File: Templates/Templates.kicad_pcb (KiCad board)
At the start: 0 parts

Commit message: update:添加文件
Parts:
- added BAT1: CR2032, DuRuofu_Connector:BAT-TH_BS-2-1, F.Cu at (105.1, 46.4)
- added J1: DC-005, EXT_Connectors_THT:DC-005, F.Cu at (107.6, 59.8)
- added J10: ~, EXT_Other:ANT-SMD_L3.1-W1.6, F.Cu at (135.4, 108.8)
- added J2: ~, Connector_Coaxial:U.FL_Hirose_U.FL-R-SMT-1_Vertical, F.Cu at (148.0, 43.9)
- added J3: Micro_SD_Card, EXT_Connectors_SMD:自弹式micro-SD卡(TF卡)卡座-外焊式, F.Cu at (124.4, 80.6)
- added J4: ~, EXT_Connectors_SMD:自弹式micro-SIM卡-卡座-6P-SIM卡连接器SMD, F.Cu at (126.3, 49.7)
- added J5: ~, EXT_Connectors_THT:SMA-KWE, F.Cu at (140.6, 53.4)
- added J6: ~, EXT_Connectors_THT:CONN-TH_2P-P5.08, F.Cu at (107.8, 79.6)
- added J7: ~, EXT_Connectors_THT:CONN-TH_3P-P5.08, F.Cu at (142.7, 79.6)
- added J8: ~, EXT_Connectors_THT:CONN-TH_4P-P5.08_KF2EDGRC-5.08-4P, F.Cu at (128.4, 61.3)
- added J9: OK-14F024-04, EXT_Connectors_SMD:亚奇连接器-OK-14F024-04, F.Cu at (98.2, 79.6)
- added K1: G6K-2F-Y_DC5, DuRuofu_Switch:G6K-2F-Y DC5, F.Cu at (125.2, 97.5)
- added K2: HF32F-G-HS, EXT_Switch_THT:HF32F-G-HS, F.Cu at (103.1, 124.0)
- added OLED1: OLED_0.96, EXT_Modules:0.96OLED_4P, F.Cu at (168.6, 34.4)
- added Q1: S8050, Package_TO_SOT_SMD:SOT-23, F.Cu at (134.8, 116.0)
- added U1: ~, EXT_Connectors_THT:CONN-TH_XY2500V-F-3.5-8P, F.Cu at (131.9, 37.2)
- added U10: ~, Package_LGA:Bosch_LGA-14_3x2.5mm_P0.5mm, F.Cu at (190.5, 111.9)
- added U11: ~, EXT_IC_SMD:SMD-4_4.6x7.62mm_P2.54mm, F.Cu at (183.6, 106.5)
- added U12: RG-02, EXT_IC_SMD:GPS-SMD_GP-02, F.Cu at (189.2, 92.6)
- added U13: L9119S, Package_SO:SOP-8_5.28x5.23mm_P1.27mm, F.Cu at (182.8, 113.0)
- added U14: ~, EXT_IC_SMD:Maxim_OLGA-14_3.3x5.6mm_P0.8mm, F.Cu at (175.0, 125.6)
- added U15: MAX98357A, EXT_IC_SMD:TQFN-16-1EP_3x3mm_P0.5mm_EP1.23x1.23mm, F.Cu at (180.2, 125.7)
- added U16: Ra-01SC, EXT_IC_SMD:COMM-SMD_RA-01S, F.Cu at (162.5, 116.6)
- added U17: SGM2209, Package_TO_SOT_SMD:SOT-23-5, F.Cu at (175.0, 105.8)
- added U18: SGM2211, Package_TO_SOT_SMD:SOT-23-5, F.Cu at (175.0, 110.5)
- added U19: SGM2212-3.3XKC3G/TR, Package_TO_SOT_SMD:SOT-223, F.Cu at (177.4, 91.0)
- added U2: ~, EXT_Modules:MPU6050-GY-521, F.Cu at (185.0, 33.0)
- added U20: SGM2212-5.0XKC3G/TR, Package_TO_SOT_SMD:SOT-223, F.Cu at (177.4, 99.3)
- added U21: SGM3209YS8G/TR, Package_SO:HSOP-8-1EP_3.9x4.9mm_P1.27mm_EP2.41x3.1mm, F.Cu at (190.4, 126.4)
- added U22: SGM6601, Package_TO_SOT_SMD:TSOT-23-5, F.Cu at (175.0, 115.1)
- added U23: ~, Package_TO_SOT_SMD:SOT-23-6, F.Cu at (175.0, 119.7)
- added U24: TP4056, EXT_IC_SMD:EPSOP-8, F.Cu at (190.4, 119.8)
- added U25: TPS5430DDA, Package_SO:TI_SO-PowerPAD-8_ThermalVias, F.Cu at (181.9, 119.8)
- added U26: ~, EXT_Switch_THT:SW_Push_1P1T_NO_6x6mm, F.Cu at (118.5, 122.1)
- added U27: ~, EXT_Switch_THT:热插拔键盘轴(RGB反贴)(30mm), F.Cu at (106.7, 105.0)
- added U3: ~, EXT_Modules:MQ-2, F.Cu at (159.9, 69.4)
- added U4: ~, EXT_Modules:SW-TH_THB001P, F.Cu at (183.0, 73.6)
- added U5: ~, EXT_Other:Buzzer, F.Cu at (136.2, 99.4)
- added U6: AIR780EX, EXT_IC_SMD:LCC-54_L17.7-W15.8-P1.10_AIR780EX, F.Cu at (163.1, 97.1)
- added U7: ~, EXT_IC_SMD:WSOF-6_L2.6-W1.6-P0.50-TL-EP, F.Cu at (184.9, 99.9)
- added U8: ~, Package_LGA:Bosch_LGA-8_2.5x2.5mm_P0.65mm_ClockwisePinNumbering, F.Cu at (191.8, 105.7)
- added U9: ~, EXT_IC_SMD:WLCSP-12_1.56x1.56mm_P0.4mm, F.Cu at (189.1, 100.4)
- added X1: YSX321SL, Crystal:Crystal_SMD_SeikoEpson_FA238-4Pin_3.2x2.5mm, F.Cu at (141.0, 109.3)
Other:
- board outline added: 115.6 x 106.7 mm
- copper layers 0 -> 2

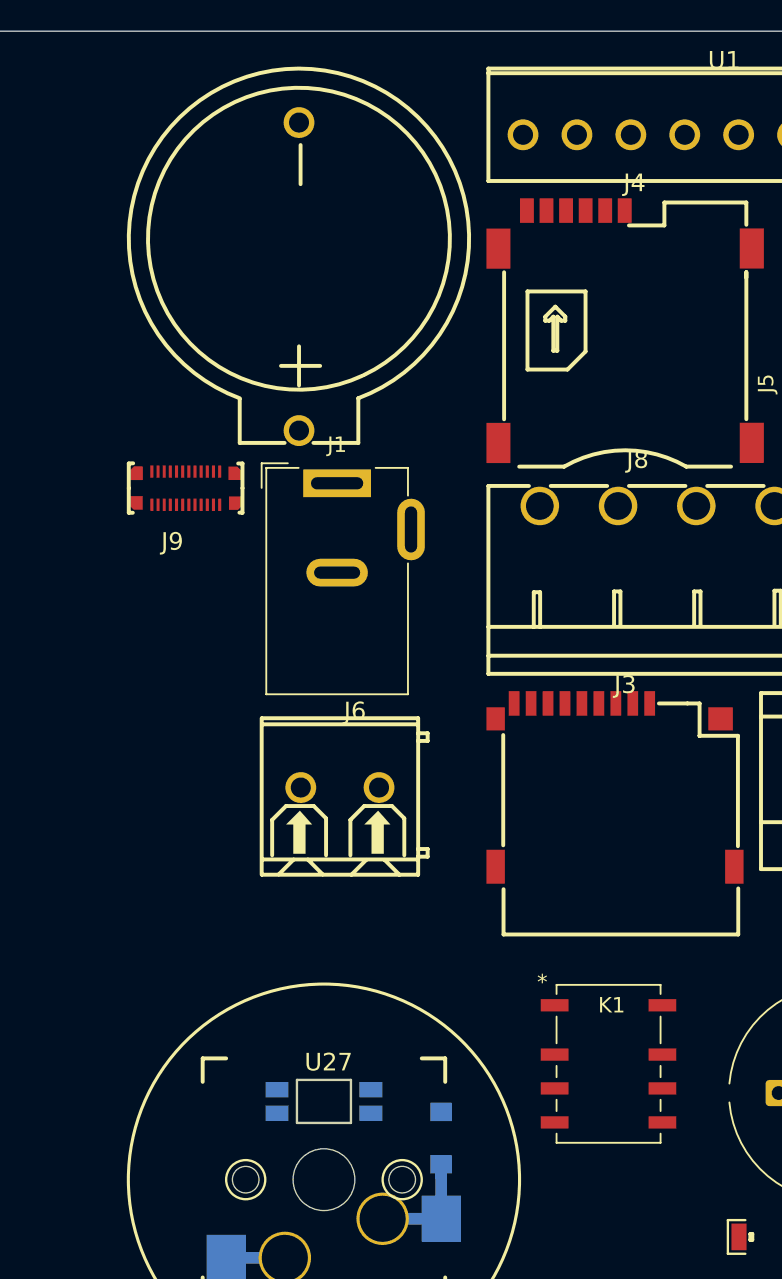
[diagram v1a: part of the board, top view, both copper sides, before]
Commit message: update: 修复库文件缺失
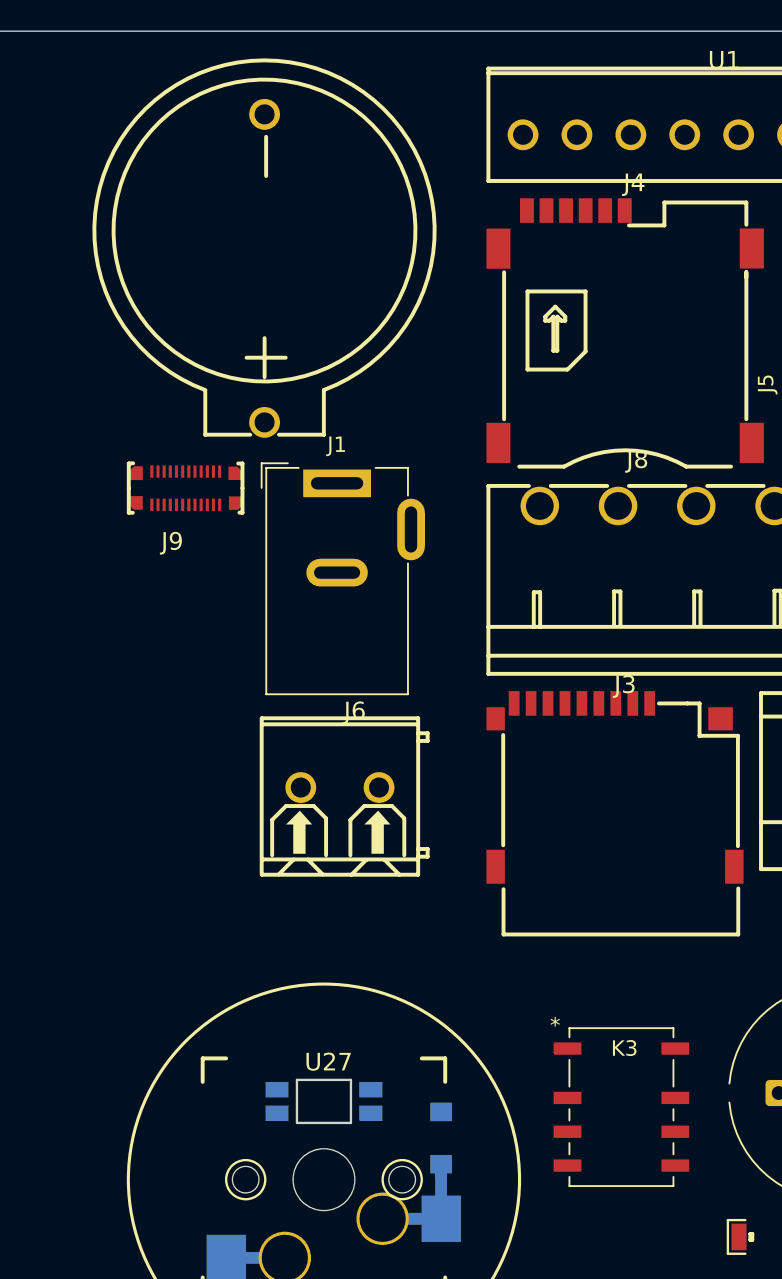
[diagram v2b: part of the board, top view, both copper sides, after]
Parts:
- removed BAT1: CR2032, DuRuofu_Connector:BAT-TH_BS-2-1
- removed K1: G6K-2F-Y_DC5, DuRuofu_Switch:G6K-2F-Y DC5
- added BAT2: CR2032, EXT_Connectors_THT:BAT-TH_BS-2-1, F.Cu at (102.9, 45.9)
- added K3: G6K-2F-Y_DC5, EXT_Switch_SMD:G6K-2F-Y DC5, F.Cu at (126.0, 100.3)

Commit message: update: 添加器件-合宙ESP32S3开发板
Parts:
- added U28: ~, EXT_Modules:合宙ESP32C3开发板-DIP&SMT, F.Cu at (292.4, 110.5)
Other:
- board size 115.6 x 106.7 mm -> 235 x 106.7 mm

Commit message: fix: 升级到9.0
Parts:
- moved U28 64.2 mm to (228.6, 103.6)
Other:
- board size 235 x 106.7 mm -> 161.3 x 106.7 mm
